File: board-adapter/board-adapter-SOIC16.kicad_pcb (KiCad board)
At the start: 2 copper layers, 10 x 11 mm, 9 parts, among them J101 Conn_01x01_Female, J102 Conn_01x01_Female, J103 Conn_01x01_Female, J104 Conn_01x01_Female, J105 Conn_01x01_Female, J106 Conn_01x01_Female, J107 Conn_01x01_Female, J108 Conn_01x01_Female, J109 Conn_02x04_Odd_Even

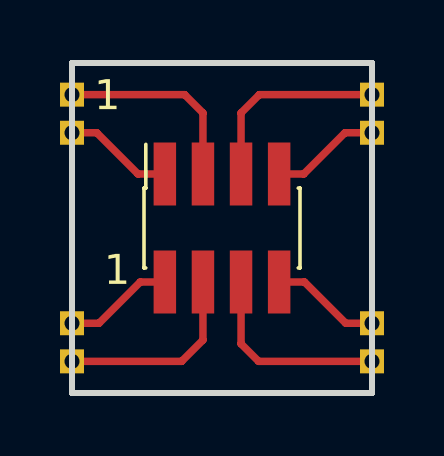
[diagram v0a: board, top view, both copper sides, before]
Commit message: increase trace width
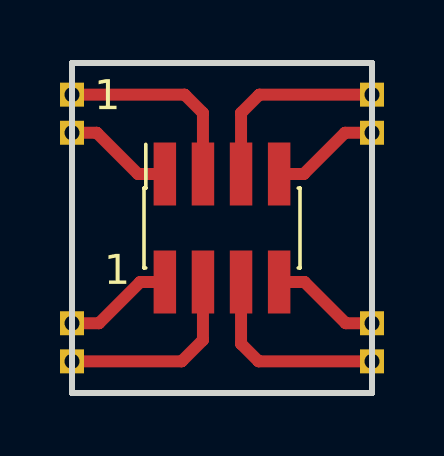
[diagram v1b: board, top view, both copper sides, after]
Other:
- net class Default: trace_width 0.25 -> 0.4; via_dia 0.8 -> 0.6; via_drill 0.4 -> 0.3
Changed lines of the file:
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@@
   )
   (setup
-    (last_trace_width 0.25)
+    (last_trace_width 0.4)
     (trace_clearance 0.2)
     (zone_clearance 0.508)
@@
     (segment_width 0.15)
     (edge_width 0.2)
-    (via_size 0.8)
-    (via_drill 0.4)
+    (via_size 0.6)
+    (via_drill 0.3)
     (via_min_size 0.4)
     (via_min_drill 0.3)
@@
     (pcbplotparams
       (layerselection 0x010fc_ffffffff)
-      (usegerberextensions false)
+      (usegerberextensions true)
       (usegerberattributes false)
       (usegerberadvancedattributes false)
@@
       (outputformat 1)
       (mirror false)
-      (drillshape 1)
+      (drillshape 0)
       (scaleselection 1)
       (outputdirectory ""))
@@
   (net_class Default "This is the default net class."
     (clearance 0.2)
-    (trace_width 0.25)
-    (via_dia 0.8)
-    (via_drill 0.4)
+    (trace_width 0.4)
+    (via_dia 0.6)
+    (via_drill 0.3)
     (uvia_dia 0.3)
     (uvia_drill 0.1)
@@
   (gr_line (start 105 94.5) (end 105 105.5) (layer Edge.Cuts) (width 0.2))
   (gr_line (start 95 94.5) (end 105 94.5) (layer Edge.Cuts) (width 0.2))
-  (segment (start 97.2 98.2) (end 98.095 98.2) (width 0.25) (layer F.Cu) (net 1))
-  (segment (start 95.825 96.825) (end 97.2 98.2) (width 0.25) (layer F.Cu) (net 1))
-  (segment (start 95 96.825) (end 95.825 96.825) (width 0.25) (layer F.Cu) (net 1))
-  (segment (start 97.275 101.8) (end 98.095 101.8) (width 0.25) (layer F.Cu) (net 2))
-  (segment (start 95.9 103.175) (end 97.275 101.8) (width 0.25) (layer F.Cu) (net 2))
-  (segment (start 95 103.175) (end 95.9 103.175) (width 0.25) (layer F.Cu) (net 2))
-  (segment (start 95 95.555) (end 98.755 95.555) (width 0.25) (layer F.Cu) (net 3))
-  (segment (start 98.755 95.555) (end 99.365 96.165) (width 0.25) (layer F.Cu) (net 3))
-  (segment (start 99.365 96.165) (end 99.365 98.2) (width 0.25) (layer F.Cu) (net 3))
-  (segment (start 95 104.445) (end 98.655 104.445) (width 0.25) (layer F.Cu) (net 4))
-  (segment (start 99.365 103.735) (end 99.365 101.8) (width 0.25) (layer F.Cu) (net 4))
-  (segment (start 98.655 104.445) (end 99.365 103.735) (width 0.25) (layer F.Cu) (net 4))
-  (segment (start 105 95.555) (end 101.245 95.555) (width 0.25) (layer F.Cu) (net 5))
-  (segment (start 101.245 95.555) (end 100.635 96.165) (width 0.25) (layer F.Cu) (net 5))
-  (segment (start 100.635 96.165) (end 100.635 98.2) (width 0.25) (layer F.Cu) (net 5))
-  (segment (start 100.635 103.86) (end 100.635 101.8) (width 0.25) (layer F.Cu) (net 6))
-  (segment (start 101.22 104.445) (end 100.635 103.86) (width 0.25) (layer F.Cu) (net 6))
-  (segment (start 105 104.445) (end 101.22 104.445) (width 0.25) (layer F.Cu) (net 6))
-  (segment (start 102.725 98.2) (end 101.905 98.2) (width 0.25) (layer F.Cu) (net 7))
-  (segment (start 104.1 96.825) (end 102.725 98.2) (width 0.25) (layer F.Cu) (net 7))
-  (segment (start 105 96.825) (end 104.1 96.825) (width 0.25) (layer F.Cu) (net 7))
-  (segment (start 104.125 103.175) (end 105 103.175) (width 0.25) (layer F.Cu) (net 8))
-  (segment (start 102.75 101.8) (end 104.125 103.175) (width 0.25) (layer F.Cu) (net 8))
-  (segment (start 101.905 101.8) (end 102.75 101.8) (width 0.25) (layer F.Cu) (net 8))
+  (segment (start 97.2 98.2) (end 98.095 98.2) (width 0.4) (layer F.Cu) (net 1))
+  (segment (start 95.825 96.825) (end 97.2 98.2) (width 0.4) (layer F.Cu) (net 1))
+  (segment (start 95 96.825) (end 95.825 96.825) (width 0.4) (layer F.Cu) (net 1))
+  (segment (start 97.275 101.8) (end 98.095 101.8) (width 0.4) (layer F.Cu) (net 2))
+  (segment (start 95.9 103.175) (end 97.275 101.8) (width 0.4) (layer F.Cu) (net 2))
+  (segment (start 95 103.175) (end 95.9 103.175) (width 0.4) (layer F.Cu) (net 2))
+  (segment (start 95 95.555) (end 98.755 95.555) (width 0.4) (layer F.Cu) (net 3))
+  (segment (start 98.755 95.555) (end 99.365 96.165) (width 0.4) (layer F.Cu) (net 3))
+  (segment (start 99.365 96.165) (end 99.365 98.2) (width 0.4) (layer F.Cu) (net 3))
+  (segment (start 95 104.445) (end 98.655 104.445) (width 0.4) (layer F.Cu) (net 4))
+  (segment (start 99.365 103.735) (end 99.365 101.8) (width 0.4) (layer F.Cu) (net 4))
+  (segment (start 98.655 104.445) (end 99.365 103.735) (width 0.4) (layer F.Cu) (net 4))
+  (segment (start 105 95.555) (end 101.245 95.555) (width 0.4) (layer F.Cu) (net 5))
+  (segment (start 101.245 95.555) (end 100.635 96.165) (width 0.4) (layer F.Cu) (net 5))
+  (segment (start 100.635 96.165) (end 100.635 98.2) (width 0.4) (layer F.Cu) (net 5))
+  (segment (start 100.635 103.86) (end 100.635 101.8) (width 0.4) (layer F.Cu) (net 6))
+  (segment (start 101.22 104.445) (end 100.635 103.86) (width 0.4) (layer F.Cu) (net 6))
+  (segment (start 105 104.445) (end 101.22 104.445) (width 0.4) (layer F.Cu) (net 6))
+  (segment (start 102.725 98.2) (end 101.905 98.2) (width 0.4) (layer F.Cu) (net 7))
+  (segment (start 104.1 96.825) (end 102.725 98.2) (width 0.4) (layer F.Cu) (net 7))
+  (segment (start 105 96.825) (end 104.1 96.825) (width 0.4) (layer F.Cu) (net 7))
+  (segment (start 104.125 103.175) (end 105 103.175) (width 0.4) (layer F.Cu) (net 8))
+  (segment (start 102.75 101.8) (end 104.125 103.175) (width 0.4) (layer F.Cu) (net 8))
+  (segment (start 101.905 101.8) (end 102.75 101.8) (width 0.4) (layer F.Cu) (net 8))
 )

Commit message: remove pin 1 markers from wrong position
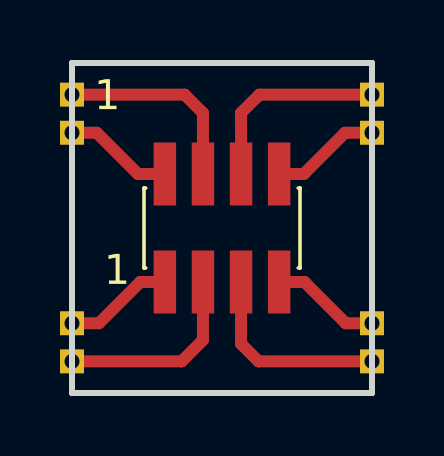
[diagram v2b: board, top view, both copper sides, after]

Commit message: update pad to mask clearance
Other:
- rule pad_to_mask_clearance: 0.2 -> 0.1
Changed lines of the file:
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@@
     (pad_size 0.8 0.8)
     (pad_drill 0.5)
-    (pad_to_mask_clearance 0.2)
+    (pad_to_mask_clearance 0.1)
     (aux_axis_origin 0 0)
     (visible_elements FFFFFF7F)
